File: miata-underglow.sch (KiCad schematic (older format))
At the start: 34 parts, among them J1 Micro_SD_Card, J2 FTDI, J3 LEDS, J4 CAN, Q1 SS8050, Q2 SS8050, U1 AMS1117-3.3, U2 TXS0108EPW, U3 AMS1117-5.0, U4 ESP32-WROOM-32D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

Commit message: Progress on routing
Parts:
- C1, C2, C3, C4: LCSC_FP (none) -> CASE-A_3216; LCSC_PN (none) -> C7171; Manufacturer Part Number (none) -> TAJA106K016RNJ
- C5, C6, C7, C8, C9: LCSC_FP (none) -> 0402; LCSC_PN (none) -> C1525; Manufacturer Part Number (none) -> CL05B104KO5NNNC
- D1, D2: LCSC_FP (none) -> 0603; LCSC_PN (none) -> C2286; Manufacturer Part Number (none) -> KT-0603R
- J1: Manufacturer Part Number (none) -> 472192001
- J2: LCSC_FP (none) -> CONN-TH_6P-P2.50_X8821WR-06K-N2SN; LCSC_PN (none) -> C397427; Manufacturer Part Number (none) -> X8821WR-06K-N2SN
- J3: LCSC_FP (none) -> CONN-TH; LCSC_PN (none) -> C157942; Manufacturer Part Number (none) -> S12B-XH-A(LF)(SN)
- J4: LCSC_FP (none) -> CONN-TH; LCSC_PN (none) -> C157928; Manufacturer Part Number (none) -> S3B-XH-A(LF)(SN)
- Q1, Q2: LCSC_FP (none) -> SOT-23-3; LCSC_PN (none) -> C2150; Manufacturer Part Number (none) -> SS8050
- R1, R2, R5, R6: LCSC_FP (none) -> 0402; LCSC_PN (none) -> C25744; Manufacturer Part Number (none) -> 0402WGF1002TCE
- R3, R4: LCSC_FP (none) -> 0603; LCSC_PN (none) -> C23138; Manufacturer Part Number (none) -> 0603WAF3300T5E
- R7: footprint Resistor_SMD:R_0402_1005Metric -> Resistor_SMD:R_1206_3216Metric; LCSC_FP (none) -> 1206; LCSC_PN (none) -> C269754; Manufacturer Part Number (none) -> RMC12061205%N
- U1: Manufacturer Part Number (none) -> AMS1117-3.3
- U2: Manufacturer Part Number (none) -> TXS0108EPWR
- U3: LCSC_PN C6186 -> C6187; Manufacturer Part Number (none) -> AMS1117-5.0
- U4: Manufacturer Part Number (none) -> ESP32-WROOM-32D
- U5: LCSC_FP (none) -> SSOP-28_5.3x10.2x0.65P; LCSC_PN (none) -> C184944; Manufacturer Part Number (none) -> MCP25625-E/SS
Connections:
- net +12V: now also J3.2 (Pin_2), J3.3 (Pin_3), J3.4 (Pin_4)
- net +3V3: now also U2.10 (OE)
- net CAN_RX1_BF: now also U4.8 (IO32); no longer U4.23 (IO15)
- net CAN_TX0_RTS: now also U4.12 (IO27); no longer U4.13 (IO14)
- net CAN_TX1_RTS: now also U4.11 (IO26); no longer U4.16 (IO13)
- net CAN_TX2_RTS: now also U4.10 (IO25); no longer U4.14 (IO12)
- net GND: now also J3.5 (Pin_5), J3.6 (Pin_6), J3.7 (Pin_7), U2.1 (A1), U2.12 (B8), U2.13 (B7), U2.14 (B6), U2.20 (B1), U2.7 (A6), U2.8 (A7), U2.9 (A8)
- net LED0: now also U2.4 (A3), U4.16 (IO13); no longer U2.1 (A1), U4.10 (IO25)
- net LED0_OUT: now also J3.10 (Pin_10), U2.17 (B3); no longer J3.8 (Pin_8), U2.20 (B1)
- net LED1: now also U4.14 (IO12); no longer U4.11 (IO26)
- net LED1_OUT: now also J3.11 (Pin_11); no longer J3.9 (Pin_9)
- net LED2: now also U2.5 (A4), U4.13 (IO14); no longer U2.4 (A3), U4.12 (IO27)
- net LED2_OUT: now also J3.9 (Pin_9), U2.16 (B4); no longer J3.10 (Pin_10), U2.17 (B3)
- net LED3: now also U2.6 (A5), U4.23 (IO15); no longer U2.5 (A4), U4.8 (IO32)
- net LED3_OUT: now also J3.8 (Pin_8), U2.15 (B5); no longer J3.11 (Pin_11), U2.16 (B4)
- no-connect marks 25 -> 11
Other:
- moved on the sheet: J3

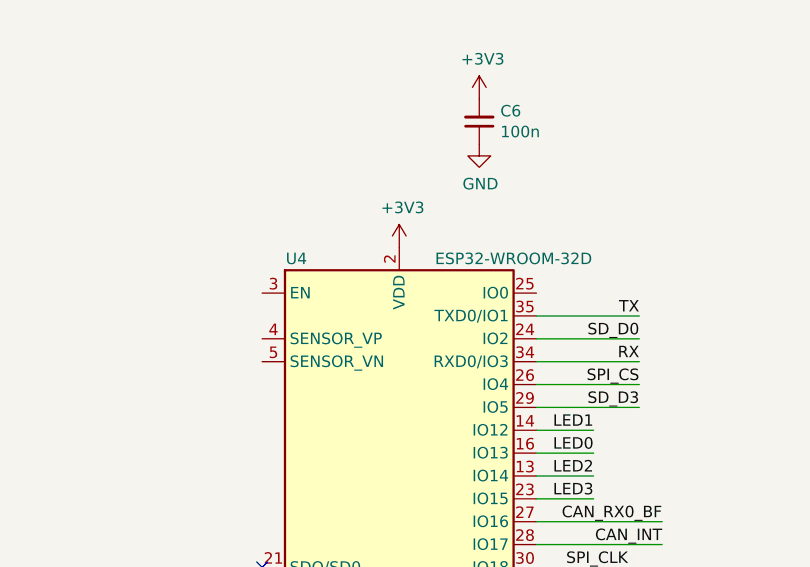
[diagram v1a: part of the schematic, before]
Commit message: More routing progress
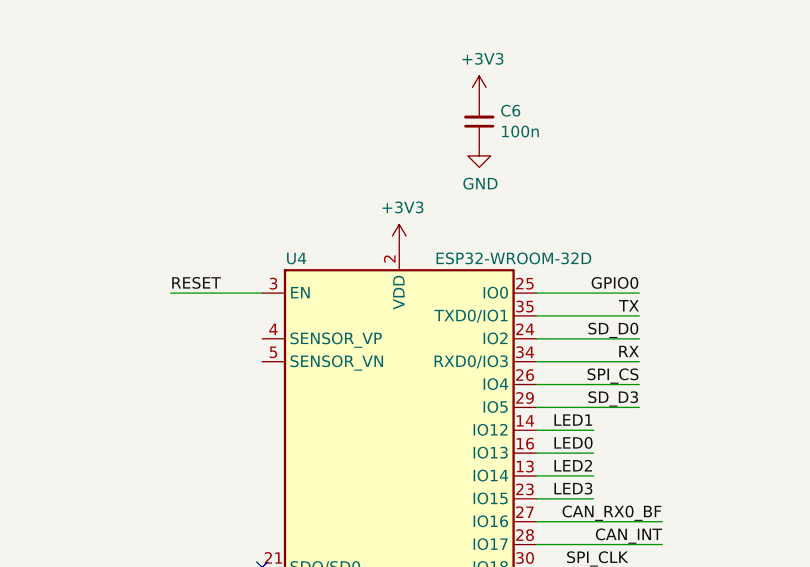
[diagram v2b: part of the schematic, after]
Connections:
- net GPIO0: now also U4.25 (IO0)
- net RESET: now also U4.3 (EN)
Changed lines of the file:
@@
 	2250 4850 2000 4850
 Connection ~ 2000 4850
+Text Label 6550 3050 2    50   ~ 0
+GPIO0
+Wire Wire Line
+	6550 3050 6100 3050
+Wire Wire Line
+	4500 3050 4900 3050
+Text Label 4500 3050 0    50   ~ 0
+RESET
 $EndSCHEMATC
